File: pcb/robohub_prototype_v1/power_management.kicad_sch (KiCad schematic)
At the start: 121 parts, among them J21 Barrel_Jack_Switch_Pin3Ring, U21 LM3880, U22 TPS564242DRL, U23 TPS564242DRL, U24 TPS564242DRL, U25 TPS564242DRL, U26 TPS564242DRL, U27 TPS564242DRL

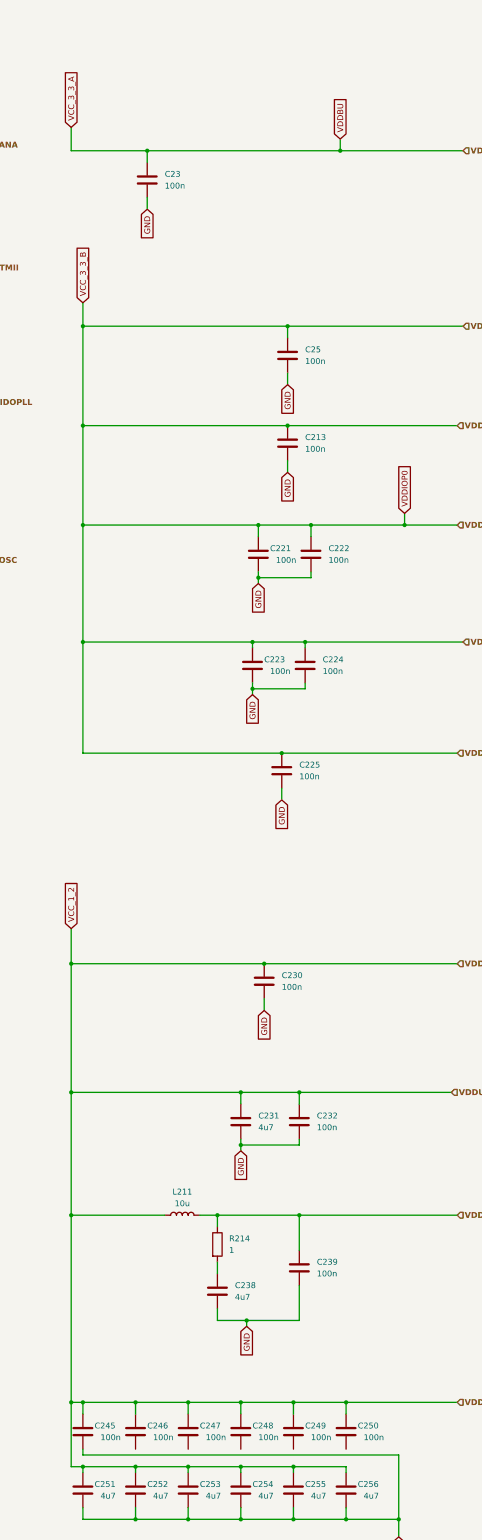
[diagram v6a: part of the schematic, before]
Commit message: Start routing ddr2
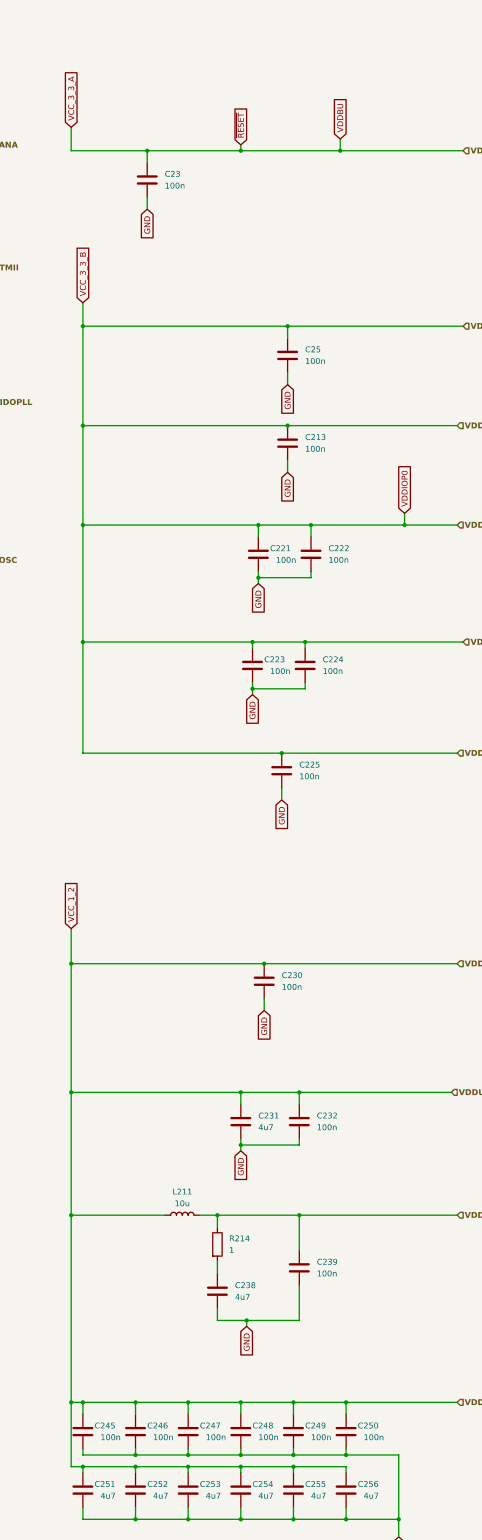
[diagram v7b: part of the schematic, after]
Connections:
- net GND: now also C246.2, C247.2, C248.2, C249.2, C250.2
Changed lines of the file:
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@@
 	)
 	(junction
+		(at 342.9 368.3)
+		(diameter 0)
+		(color 0 0 0 0)
+	)
+	(junction
 		(at 364.49 426.72)
 		(diameter 0)
@@
 	)
 	(junction
+		(at 377.19 368.3)
+		(diameter 0)
+		(color 0 0 0 0)
+	)
+	(junction
 		(at 358.14 166.37)
 		(diameter 0)
@@
 	)
 	(junction
+		(at 354.33 368.3)
+		(diameter 0)
+		(color 0 0 0 0)
+	)
+	(junction
 		(at 320.04 144.78)
 		(diameter 0)
@@
 	)
 	(junction
+		(at 354.33 85.09)
+		(diameter 0)
+		(color 0 0 0 0)
+	)
+	(junction
 		(at 128.27 147.32)
 		(diameter 0)
@@
 	)
 	(junction
+		(at 331.47 368.3)
+		(diameter 0)
+		(color 0 0 0 0)
+	)
+	(junction
 		(at 111.76 332.74)
 		(diameter 0)
@@
 	)
 	(junction
+		(at 365.76 368.3)
+		(diameter 0)
+		(color 0 0 0 0)
+	)
+	(junction
 		(at 111.76 317.5)
 		(diameter 0)
@@
 	(wire
 		(pts
+			(xy 331.47 368.3) (xy 342.9 368.3)
+		)
+		(stroke
+			(width 0)
+			(type default)
+		)
+	)
+	(wire
+		(pts
 			(xy 354.33 379.73) (xy 354.33 382.27)
 		)
@@
 	(wire
 		(pts
+			(xy 365.76 367.03) (xy 365.76 368.3)
+		)
+		(stroke
+			(width 0)
+			(type default)
+		)
+	)
+	(wire
+		(pts
 			(xy 99.06 374.65) (xy 99.06 359.41)
 		)
@@
 	(wire
 		(pts
+			(xy 377.19 367.03) (xy 377.19 368.3)
+		)
+		(stroke
+			(width 0)
+			(type default)
+		)
+	)
+	(wire
+		(pts
 			(xy 353.06 412.75) (xy 364.49 412.75)
 		)
@@
 	(wire
 		(pts
+			(xy 331.47 367.03) (xy 331.47 368.3)
+		)
+		(stroke
+			(width 0)
+			(type default)
+		)
+	)
+	(wire
+		(pts
+			(xy 354.33 83.82) (xy 354.33 85.09)
+		)
+		(stroke
+			(width 0)
+			(type default)
+		)
+	)
+	(wire
+		(pts
 			(xy 135.89 508) (xy 135.89 516.89)
 		)
@@
 	(wire
 		(pts
+			(xy 342.9 367.03) (xy 342.9 368.3)
+		)
+		(stroke
+			(width 0)
+			(type default)
+		)
+	)
+	(wire
+		(pts
 			(xy 92.71 441.96) (xy 92.71 453.39)
 		)
@@
 	(wire
 		(pts
+			(xy 377.19 368.3) (xy 388.62 368.3)
+		)
+		(stroke
+			(width 0)
+			(type default)
+		)
+	)
+	(wire
+		(pts
 			(xy 212.09 364.49) (xy 212.09 375.92)
 		)
@@
 	(wire
 		(pts
-			(xy 375.92 85.09) (xy 334.01 85.09)
+			(xy 375.92 85.09) (xy 354.33 85.09)
 		)
 		(stroke
@@
 	(wire
 		(pts
-			(xy 320.04 368.3) (xy 388.62 368.3)
+			(xy 320.04 368.3) (xy 331.47 368.3)
 		)
 		(stroke
@@
 	(wire
 		(pts
+			(xy 354.33 367.03) (xy 354.33 368.3)
+		)
+		(stroke
+			(width 0)
+			(type default)
+		)
+	)
+	(wire
+		(pts
 			(xy 104.14 147.32) (xy 114.3 147.32)
 		)
@@
 	(wire
 		(pts
+			(xy 354.33 85.09) (xy 334.01 85.09)
+		)
+		(stroke
+			(width 0)
+			(type default)
+		)
+	)
+	(wire
+		(pts
 			(xy 99.06 382.27) (xy 99.06 393.7)
 		)
@@
 		)
 	)
+	(wire
+		(pts
+			(xy 342.9 368.3) (xy 354.33 368.3)
+		)
+		(stroke
+			(width 0)
+			(type default)
+		)
+	)
 	(polyline
 		(pts
@@
 		)
 	)
+	(wire
+		(pts
+			(xy 354.33 368.3) (xy 365.76 368.3)
+		)
+		(stroke
+			(width 0)
+			(type default)
+		)
+	)
 	(polyline
 		(pts
@@
 	(wire
 		(pts
+			(xy 365.76 368.3) (xy 377.19 368.3)
+		)
+		(stroke
+			(width 0)
+			(type default)
+		)
+	)
+	(wire
+		(pts
 			(xy 331.47 379.73) (xy 331.47 382.27)
 		)
@@
 				(hide yes)
 			)
+		)
+	)
+	(global_label "~{RESET}"
+		(shape input)
+		(at 354.33 83.82 90)
+		(fields_autoplaced yes)
+		(effects
+			(font
+				(size 1.27 1.27)
+			)
+			(justify left)
+		)
+		(property "Intersheetrefs" "${INTERSHEET_REFS}"
+			(at 354.33 75.0897 90)
+			(effects
+				(font
+					(size 1.27 1.27)
+				)
+				(justify left)
+				(hide yes)
+			)
